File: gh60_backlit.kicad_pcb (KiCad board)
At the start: 2 copper layers, 81 x 15 mm, 10 parts, among them U1 PAM2804

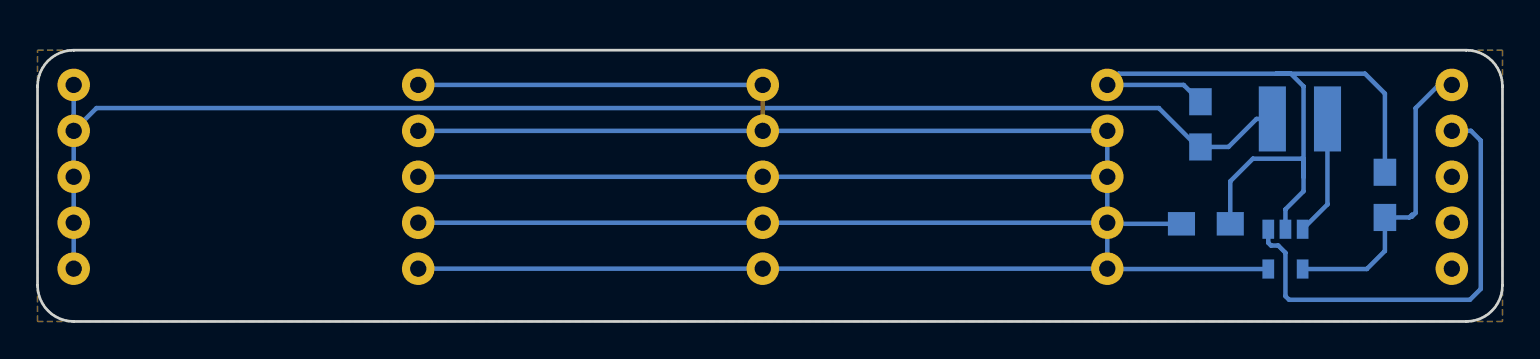
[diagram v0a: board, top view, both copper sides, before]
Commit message: Increased GND areas
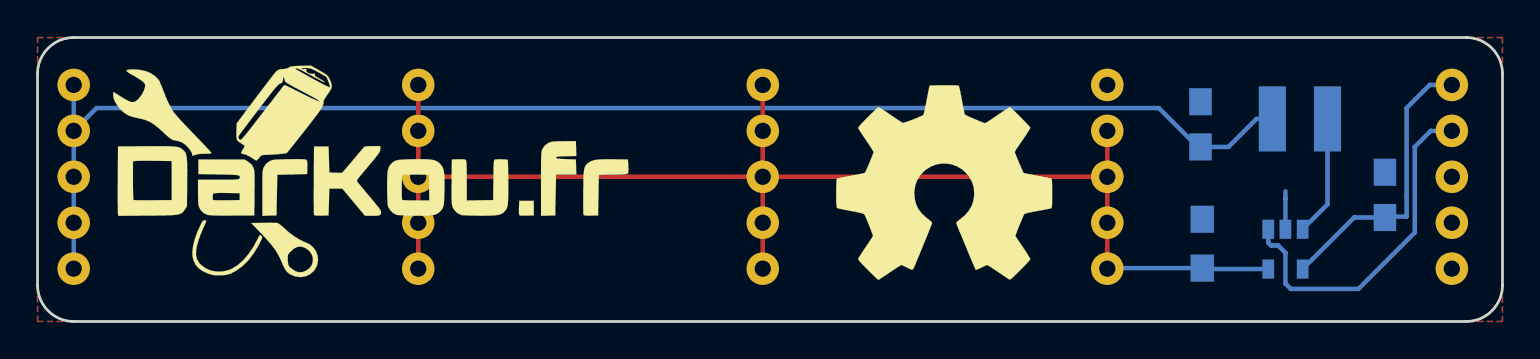
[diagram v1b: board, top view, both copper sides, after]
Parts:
- added G***: LOGO, Footprint:darkou, B.Cu at (112.5, 107.1)
- added G***: LOGO, Footprint:darkou, F.Cu at (88.2, 106.5)
- added G***: LOGO, Footprint:OPEN-HARDWARE, F.Cu at (119.9, 107.2)
- moved R1 1.12 mm to (134.2, 110.5), turned to 90 degrees
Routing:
- net LCOL1: track 194.6 -> 75.1 mm
- net GND: track 43.8 -> 2.10 mm
- net GPIO2: track 25.5 -> 19.3 mm
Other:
- board size 81 x 15 mm -> 81 x 15.7 mm
- board text added: "GH60 Backlit rev. A"

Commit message: Fixed bug on wiring
Rotated for pin header with GND and VCC.
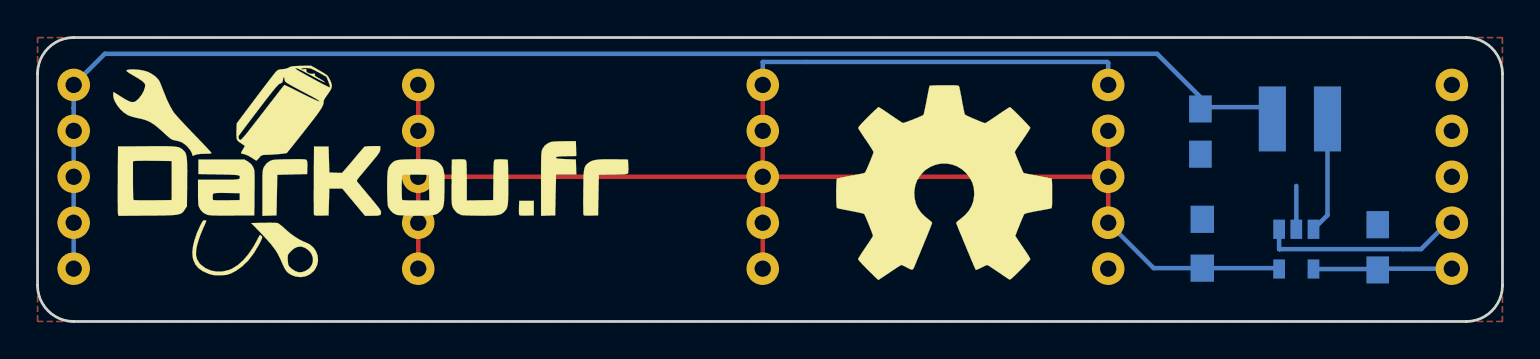
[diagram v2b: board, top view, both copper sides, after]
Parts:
- moved C1 2.93 mm to (143.9, 110.7)
- moved U1 0.60 mm to (139.4, 110.8)
- moved C2 0.40 mm to (134.1, 104.3), turned to 270 degrees
- moved 5_PIN_HEADER3 0.05 mm to (129.0, 106.8), turned to 180 degrees
- turned 5_PIN_HEADER4 to 180 degrees
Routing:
- net LCOL1: track 75.1 -> 96.5 mm
- net VCC: track 17.1 -> 7.77 mm
- net GPIO2: track 19.3 -> 11.3 mm
- net LROW1: track 78.5 -> 79.1 mm
- net GND: track 2.10 -> 2.69 mm
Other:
- board text added: "o"
